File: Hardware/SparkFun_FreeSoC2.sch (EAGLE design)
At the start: 102 parts, among them U1 CY8C5888AXI-LP035, U2 MIC5219 5V, U3 MIC5219 3.3V, U7 CY8C5868LTI-LP039, Y1 32.768kHz

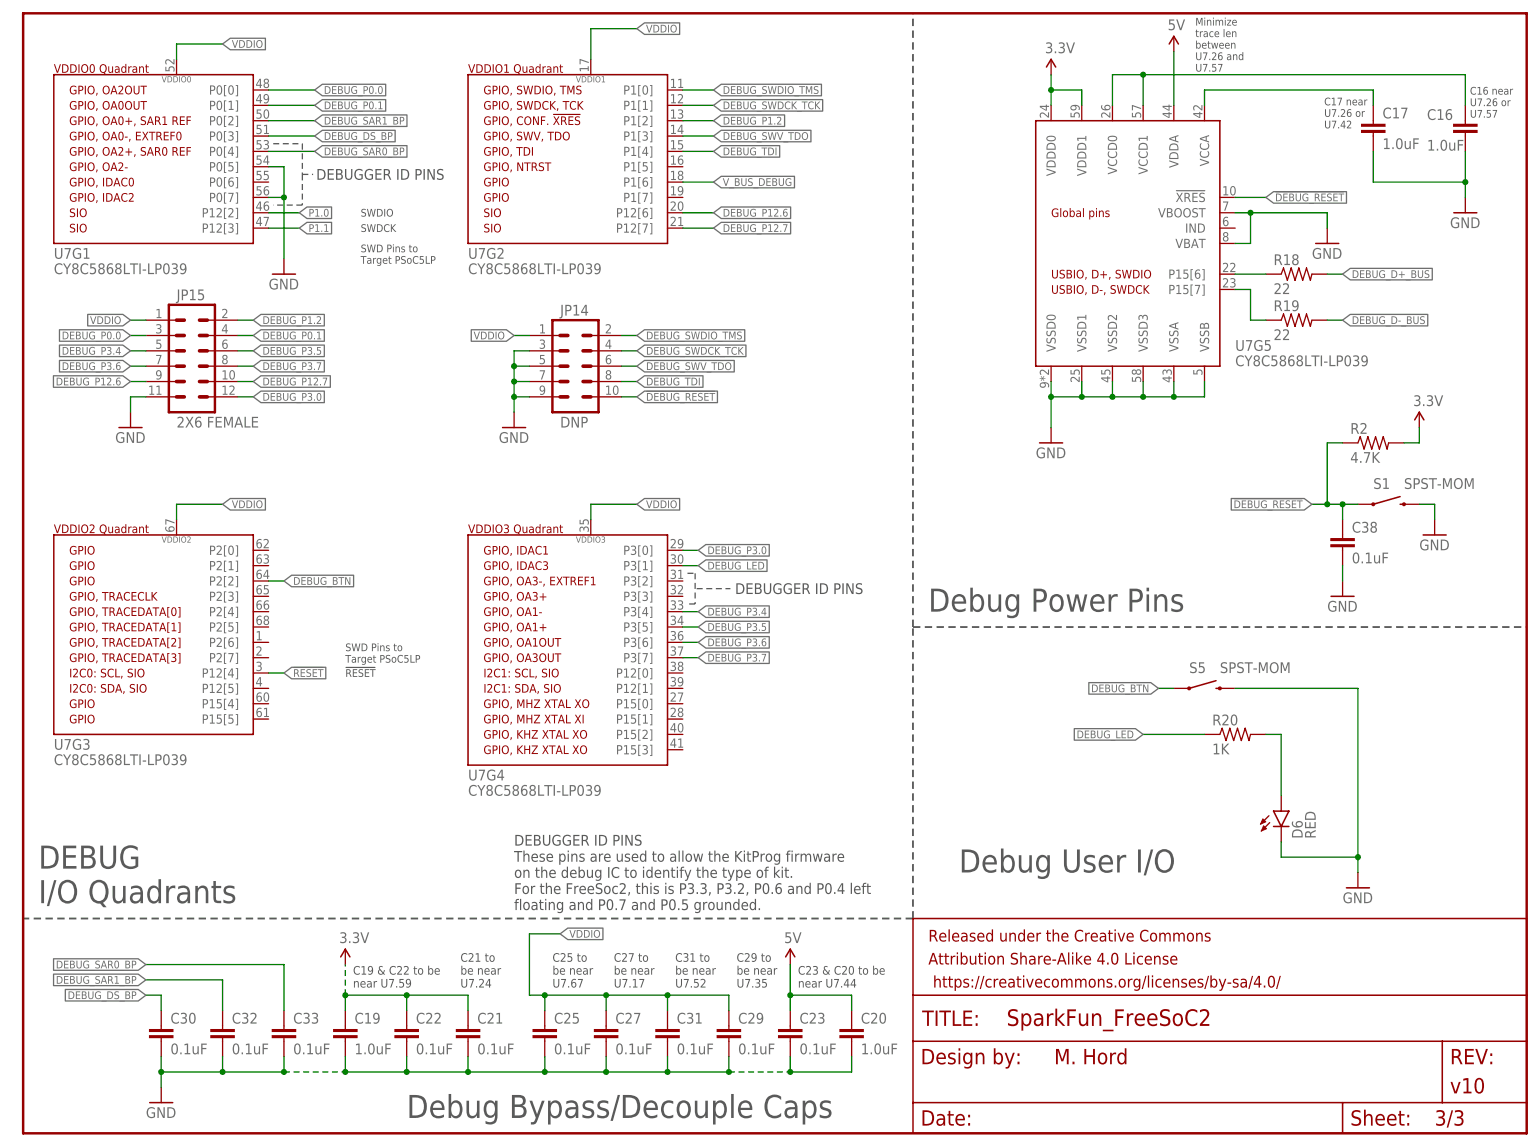
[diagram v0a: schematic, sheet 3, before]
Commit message: Add UART/I2C bridge, lock headers, IC names
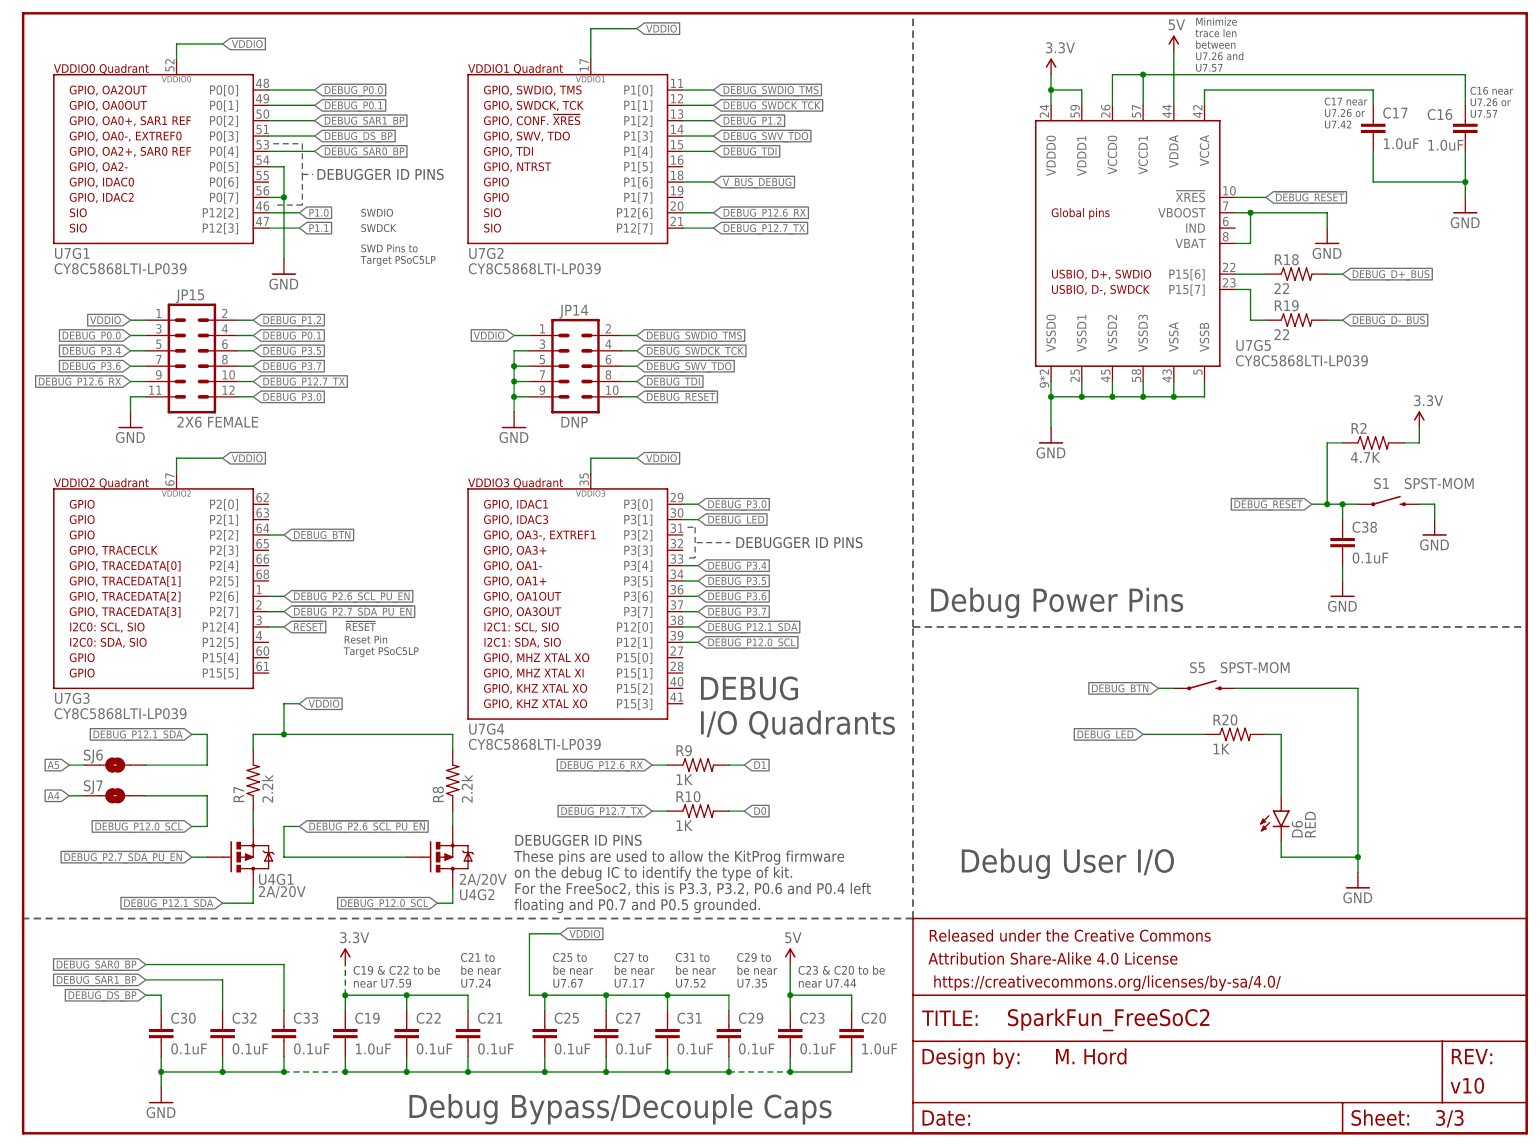
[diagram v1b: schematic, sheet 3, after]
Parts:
- added R10, R9: 1K, SparkFun-Resistors:1KOHM1/10W1%(0603)
- added R7, R8: 2.2k, SparkFun-Resistors:2.2KOHM-1/10W-1%(0603)
- added SJ6, SJ7: JUMPER-PAD-2-NO, SparkFun-Passives:JUMPER-PAD-2-NO
- added U4: 2A/20V, SparkFun-DiscreteSemi:MOSFET-PCHANNEL_DUALSOT26
- JP10, JP5, JP6: device SparkFun-Connectors:M08SILK_FEMALE_PTH -> SparkFun-Connectors:M08LOCK
- JP4: device SparkFun-Connectors:M06SILK_FEMALE_PTH -> SparkFun-Connectors:M06SIP_LOCK
- JP7: device SparkFun-Connectors:M10SILK_FEMALE_PTH -> SparkFun-Connectors:M10LOCK
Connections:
- removed net DEBUG_P12.6: JP15.9, U7G2.P12[6]
- removed net DEBUG_P12.7: JP15.10, U7G2.P12[7]
- new net !DEBUG_P2.6_SCL_PU_EN: U4G2.G, U7G3.P2[6]
- new net !DEBUG_P2.7_SDA_PU_EN: U4G1.G, U7G3.P2[7]
- new net DEBUG_P12.0_SCL: SJ7.2, U4G2.D, U7G4.P12[1]
- new net DEBUG_P12.1_SDA: SJ6.2, U4G1.D, U7G4.P12[0]
- new net DEBUG_P12.6_RX: JP15.9, R9.1, U7G2.P12[6]
- new net DEBUG_P12.7_TX: JP15.10, R10.1, U7G2.P12[7]
- new net N$7: R8.1, U4G2.S
- new net N$8: R7.1, U4G1.S
- net A4: now also SJ7.1
- net A5: now also SJ6.1
- net D0: now also R10.2
- net D1: now also R9.2
- net VDDIO: now also R7.2, R8.2
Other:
- note added: "Reset Pin Target PSoC5LP"
- moved on the sheet: U7G3, U7G4

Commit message: Revisions from QC check
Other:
- note added: "Normally open jumpers Close to connect debugger to target via I2C"
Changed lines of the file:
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@@
 <text x="53.086" y="80.772" size="1.27" layer="97" align="center-left">Reset Pin
 Target PSoC5LP</text>
+<text x="17.78" y="56.388" size="1.016" layer="97">Normally open jumpers
+Close to connect debugger
+to target via I2C</text>
 </plain>
 <instances>

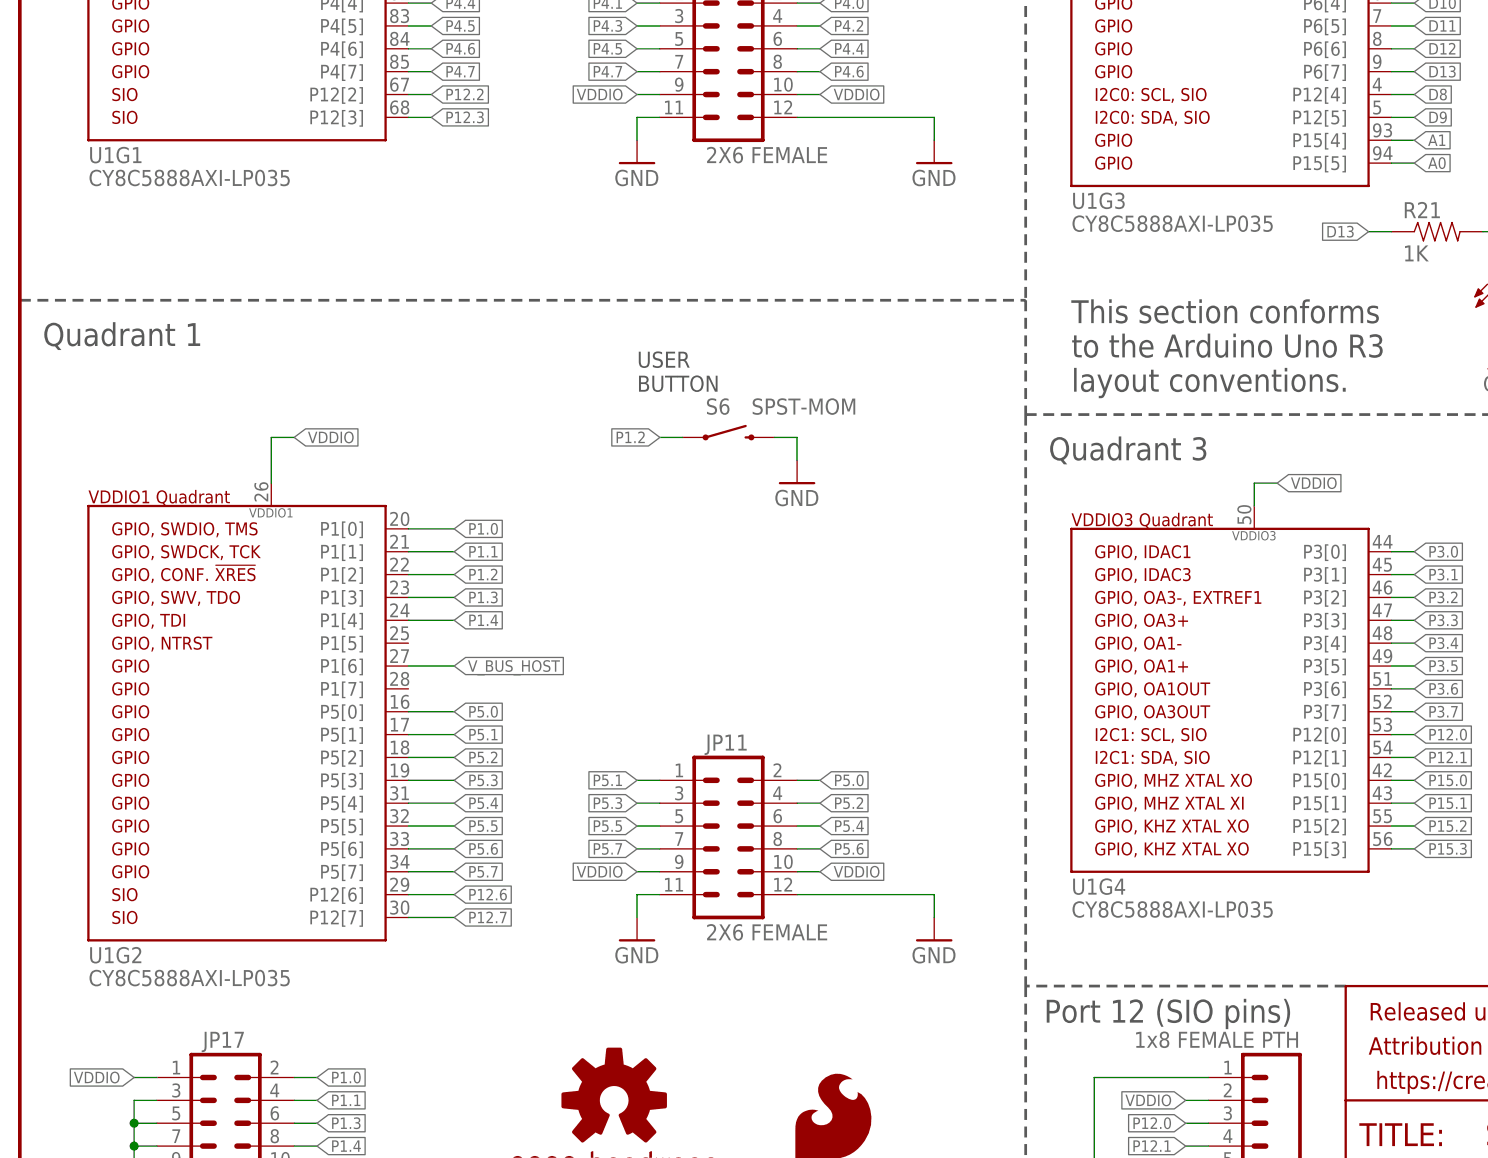
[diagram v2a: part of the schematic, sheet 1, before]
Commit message: Fixed silk/part value for target IC
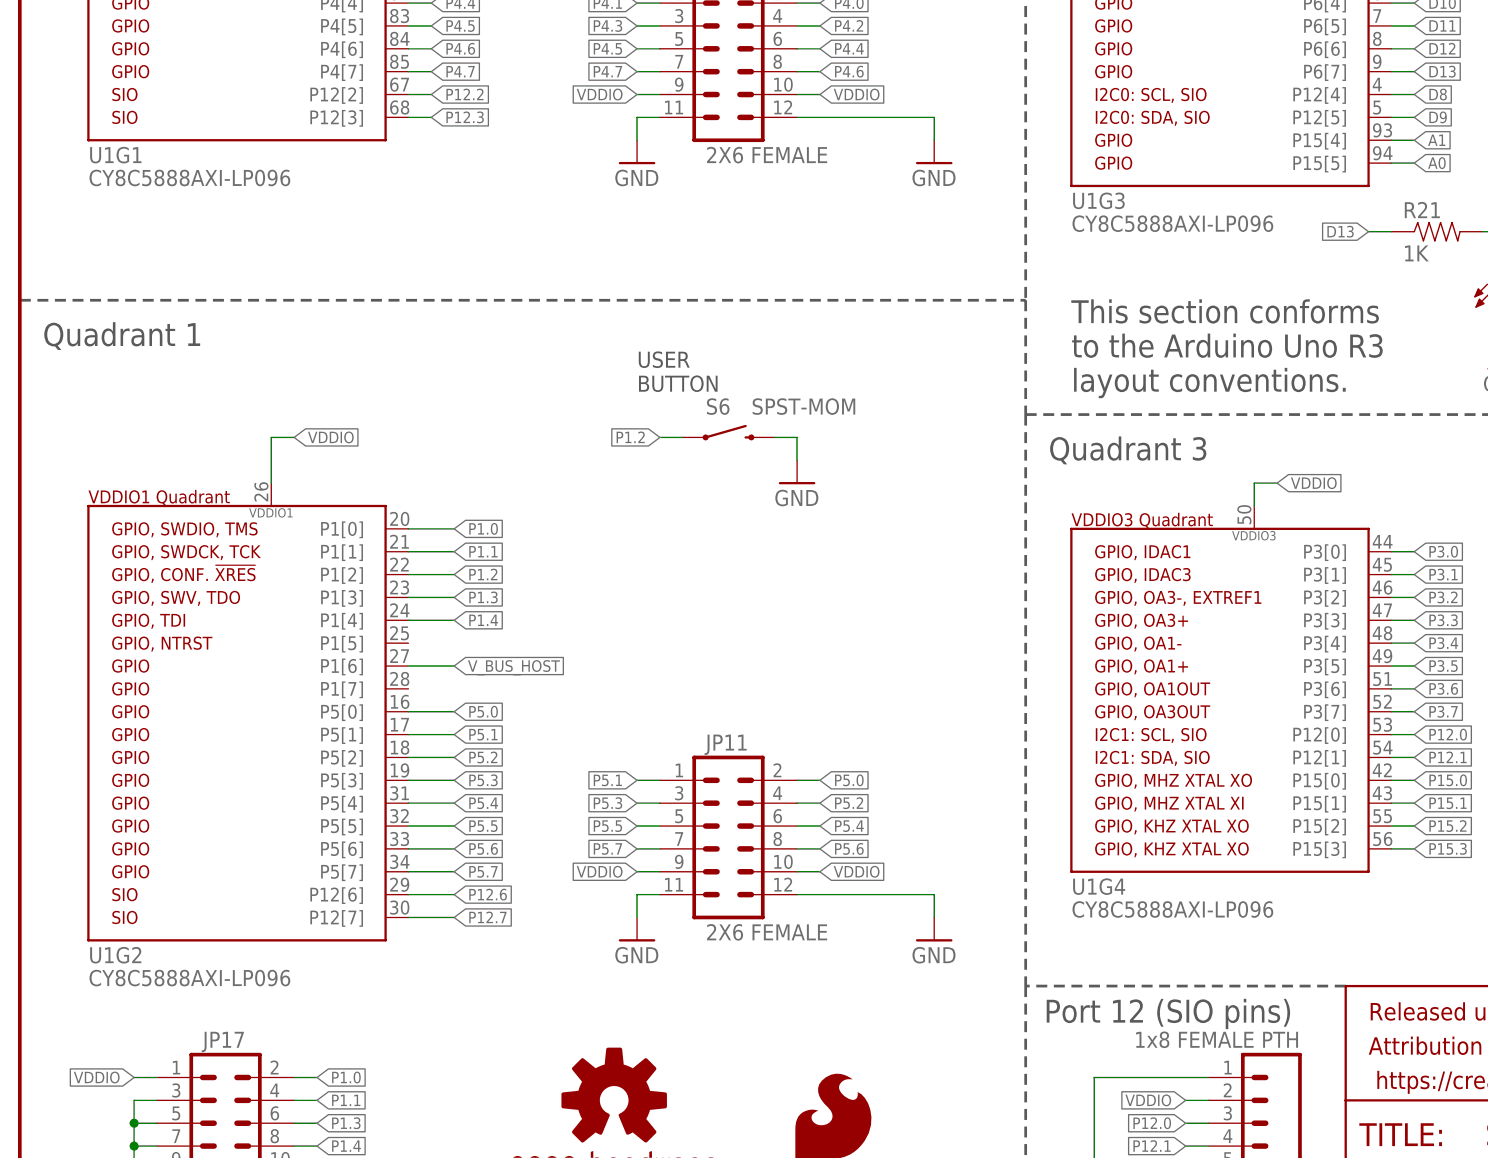
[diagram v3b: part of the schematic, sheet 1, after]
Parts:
- U1: value CY8C5888AXI-LP035 -> CY8C5888AXI-LP096
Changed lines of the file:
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@@
 <layer number="56" name="wert" color="7" fill="1" visible="no" active="no"/>
 <layer number="57" name="tCAD" color="7" fill="1" visible="no" active="no"/>
+<layer number="59" name="tCarbon" color="7" fill="1" visible="no" active="no"/>
+<layer number="60" name="bCarbon" color="7" fill="1" visible="no" active="no"/>
 <layer number="90" name="Modules" color="5" fill="1" visible="yes" active="yes"/>
 <layer number="91" name="Nets" color="2" fill="1" visible="yes" active="yes"/>
@@
 <layer number="127" name="_tValues" color="7" fill="1" visible="yes" active="yes"/>
 <layer number="128" name="_bValues" color="7" fill="1" visible="yes" active="yes"/>
+<layer number="129" name="Mask" color="7" fill="1" visible="yes" active="yes"/>
 <layer number="131" name="tAdjust" color="7" fill="1" visible="yes" active="yes"/>
 <layer number="132" name="bAdjust" color="7" fill="1" visible="yes" active="yes"/>
@@
 <attribute name="VERSION" value="v10"/>
 </part>
-<part name="U1" library="SparkFun-DigitalIC" deviceset="PSOC_5LP_100QFP" device="" value="CY8C5888AXI-LP035"/>
+<part name="U1" library="SparkFun-DigitalIC" deviceset="PSOC_5LP_100QFP" device="" value="CY8C5888AXI-LP096"/>
 <part name="D1" library="SparkFun-DiscreteSemi" deviceset="MBRA140" device=""/>
 <part name="D2" library="SparkFun-DiscreteSemi" deviceset="MBRA140" device=""/>

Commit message: Add prod_id info to some parts
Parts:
- JP10, JP5, JP6: PROD_ID (none) -> CONN-08438
- JP4: PROD_ID (none) -> CONN-08437
- JP7: PROD_ID (none) -> CONN-11563
- S3, S4: PROD_ID (none) -> SWCH-08261
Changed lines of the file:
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@@
 <part name="GND19" library="SparkFun-Aesthetics" deviceset="GND" device=""/>
 <part name="C15" library="SparkFun-Capacitors" deviceset="0.1UF-16V(+-10%)(0402)" device="" value="0.1uF"/>
-<part name="JP4" library="SparkFun-Connectors" deviceset="M06" device="SIP_LOCK" value="1X6 FEMALE PTH"/>
-<part name="JP5" library="SparkFun-Connectors" deviceset="M08" device="LOCK" value="1X8 FEMALE PTH"/>
-<part name="JP6" library="SparkFun-Connectors" deviceset="M08" device="LOCK" value="1X8 FEMALE PTH"/>
-<part name="JP7" library="SparkFun-Connectors" deviceset="M10" device="LOCK" value="1X10 FEMALE PTH"/>
+<part name="JP4" library="SparkFun-Connectors" deviceset="M06" device="SIP_LOCK" value="1X6 FEMALE PTH">
+<attribute name="PROD_ID" value="CONN-08437"/>
+</part>
+<part name="JP5" library="SparkFun-Connectors" deviceset="M08" device="LOCK" value="1X8 FEMALE PTH">
+<attribute name="PROD_ID" value="CONN-08438"/>
+</part>
+<part name="JP6" library="SparkFun-Connectors" deviceset="M08" device="LOCK" value="1X8 FEMALE PTH">
+<attribute name="PROD_ID" value="CONN-08438"/>
+</part>
+<part name="JP7" library="SparkFun-Connectors" deviceset="M10" device="LOCK" value="1X10 FEMALE PTH">
+<attribute name="PROD_ID" value="CONN-11563"/>
+</part>
 <part name="GND21" library="SparkFun-Aesthetics" deviceset="GND" device=""/>
 <part name="GND22" library="SparkFun-Aesthetics" deviceset="GND" device=""/>
@@
 <part name="SUPPLY1" library="SparkFun-Aesthetics" deviceset="5V" device=""/>
 <part name="SUPPLY2" library="SparkFun-Aesthetics" deviceset="3.3V" device=""/>
-<part name="S3" library="SparkFun-Electromechanical" deviceset="SWITCH-SPDT" device="PTH_LOCK" value="SPDT"/>
-<part name="S4" library="SparkFun-Electromechanical" deviceset="SWITCH-SPDT" device="PTH_LOCK" value="SPDT"/>
+<part name="S3" library="SparkFun-Electromechanical" deviceset="SWITCH-SPDT" device="PTH_LOCK" value="SPDT">
+<attribute name="PROD_ID" value="SWCH-08261"/>
+</part>
+<part name="S4" library="SparkFun-Electromechanical" deviceset="SWITCH-SPDT" device="PTH_LOCK" value="SPDT">
+<attribute name="PROD_ID" value="SWCH-08261"/>
+</part>
 <part name="SUPPLY3" library="SparkFun-Aesthetics" deviceset="5V" device=""/>
 <part name="SUPPLY5" library="SparkFun-Aesthetics" deviceset="5V" device=""/>
@@
 <part name="SJ4" library="SparkFun-Passives" deviceset="JUMPER-PAD-2-NO" device=""/>
 <part name="SJ5" library="SparkFun-Passives" deviceset="JUMPER-PAD-2-NO" device=""/>
-<part name="JP10" library="SparkFun-Connectors" deviceset="M08" device="LOCK" value="1x8 FEMALE PTH"/>
+<part name="JP10" library="SparkFun-Connectors" deviceset="M08" device="LOCK" value="1x8 FEMALE PTH">
+<attribute name="PROD_ID" value="CONN-08438"/>
+</part>
 <part name="GND20" library="SparkFun-Aesthetics" deviceset="GND" device=""/>
 <part name="STANDOFF1" library="SparkFun-Electromechanical" deviceset="STAND-OFF" device=""/>
@@
 <instance part="U1" gate="G3" x="116.84" y="124.46"/>
 <instance part="U1" gate="G4" x="116.84" y="48.26"/>
-<instance part="JP4" gate="G$1" x="238.76" y="170.18" rot="R180"/>
-<instance part="JP5" gate="G$1" x="203.2" y="167.64" rot="R180"/>
-<instance part="JP6" gate="G$1" x="238.76" y="137.16" rot="R180"/>
-<instance part="JP7" gate="G$1" x="208.28" y="127" rot="R180"/>
+<instance part="JP4" gate="G$1" x="238.76" y="170.18" rot="R180">
+<attribute name="PROD_ID" x="238.76" y="170.18" size="1.778" layer="96" rot="R180" display="off"/>
+</instance>
+<instance part="JP5" gate="G$1" x="203.2" y="167.64" rot="R180">
+<attribute name="PROD_ID" x="203.2" y="167.64" size="1.778" layer="96" rot="R180" display="off"/>
+</instance>
+<instance part="JP6" gate="G$1" x="238.76" y="137.16" rot="R180">
+<attribute name="PROD_ID" x="238.76" y="137.16" size="1.778" layer="96" rot="R180" display="off"/>
+</instance>
+<instance part="JP7" gate="G$1" x="208.28" y="127" rot="R180">
+<attribute name="PROD_ID" x="208.28" y="127" size="1.778" layer="96" rot="R180" display="off"/>
+</instance>
 <instance part="GND21" gate="1" x="182.88" y="114.3"/>
 <instance part="GND22" gate="1" x="213.36" y="127"/>
@@
 <instance part="GND10" gate="1" x="175.26" y="40.64"/>
 <instance part="GND11" gate="1" x="208.28" y="40.64"/>
-<instance part="JP10" gate="G$1" x="137.16" y="17.78" rot="R180"/>
+<instance part="JP10" gate="G$1" x="137.16" y="17.78" rot="R180">
+<attribute name="PROD_ID" x="137.16" y="17.78" size="1.778" layer="96" rot="R180" display="off"/>
+</instance>
 <instance part="GND20" gate="1" x="119.38" y="5.08"/>
 <instance part="STANDOFF1" gate="G$1" x="243.84" y="25.4"/>
@@
 <attribute name="NAME" x="174.625" y="97.79" size="1.778" layer="95" rot="R180"/>
 <attribute name="VALUE" x="182.88" y="97.79" size="1.778" layer="96" rot="R180"/>
+<attribute name="PROD_ID" x="172.72" y="91.44" size="1.778" layer="96" rot="R180" display="off"/>
 </instance>
 <instance part="S4" gate="1" x="172.72" y="78.74" smashed="yes" rot="R180">
 <attribute name="NAME" x="174.625" y="85.09" size="1.778" layer="95" rot="R180"/>
 <attribute name="VALUE" x="182.88" y="85.09" size="1.778" layer="96" rot="R180"/>
+<attribute name="PROD_ID" x="172.72" y="78.74" size="1.778" layer="96" rot="R180" display="off"/>
 </instance>
 <instance part="SUPPLY3" gate="G$1" x="50.8" y="179.07"/>
